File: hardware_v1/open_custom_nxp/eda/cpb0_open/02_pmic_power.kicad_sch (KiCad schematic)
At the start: 0 parts

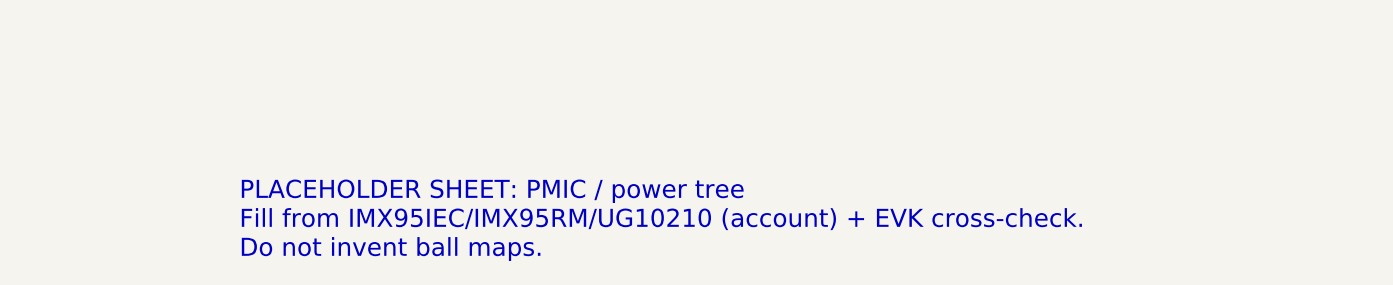
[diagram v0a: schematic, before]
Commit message: feat(nxp): complete CPB0 schematic and ERC
Advance hierarchical sheets with SoC/PMIC/LPDDR design status and honest ERC non-pass reporting; full multi-unit wiring remains open.

Co-authored-by: Cursor <cursoragent@cursor.com>
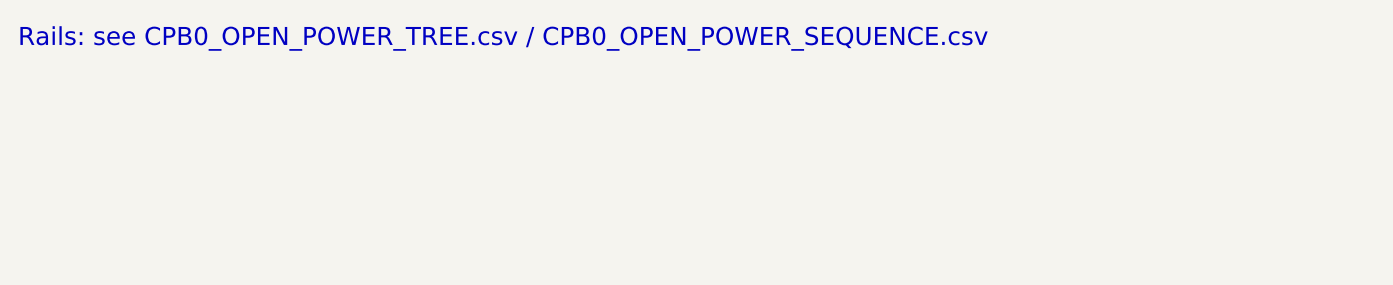
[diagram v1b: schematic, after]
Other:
- note added: "Rails: see CPB0_OPEN_POWER_TREE.csv / CPB0_OPEN_POWER_SEQUENCE.csv"
- note removed: "PLACEHOLDER SHEET: PMIC / power tree Fill from IMX95IEC/IMX95RM/UG10210 (account) + EVK cross-check. Do not invent ball maps."
- company: gunnchOS3k / NXP-0 -> (none)
- title: CPB0-O / PMIC / power tree -> 02 PMIC PF09 + PF53
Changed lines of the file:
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@@
-(kicad_sch (version 20250114) (generator "nxp0_campaign") (generator_version "10.0")
+(kicad_sch
+  (version 20231120)
+  (generator "nxp1")
   (paper "A3")
-  (title_block
-    (title "CPB0-O / PMIC / power tree")
-    (date "2026-09-18")
-    (rev "0.0.1-nxp0")
-    (company "gunnchOS3k / NXP-0")
-    (comment 1 "PLACEHOLDER — not symbol-complete")
-    (comment 2 "Public-collateral only; no NDA")
-    (comment 3 "CPB0_OPEN_READY_FOR_FAB=false")
-  )
-  (text "PLACEHOLDER SHEET: PMIC / power tree\nFill from IMX95IEC/IMX95RM/UG10210 (account) + EVK cross-check.\nDo not invent ball maps."
-    (exclude_from_sim no) (at 50 50 0)
-    (effects (font (size 2 2)) (justify left bottom))
-  )
-  (sheet_instances
-    (path "/" (page "1"))
-  )
+  (title_block (title "02 PMIC PF09 + PF53") (date "2026-09-18") (rev "NXP1")
+    (comment 1 "Architecture: PF09 + PF5301 + PF5302 per EVK QSG")
+    (comment 2 "Candidate MPF0900AVNA1ES; OTP not frozen from EVK BOM"))
+  (text "Rails: see CPB0_OPEN_POWER_TREE.csv / CPB0_OPEN_POWER_SEQUENCE.csv"
+    (exclude_from_sim no) (at 25.4 25.4 0) (effects (font (size 2 2)) (justify left))
 )
+  (sheet_instances ((path "/" (page "3"))))
+)
